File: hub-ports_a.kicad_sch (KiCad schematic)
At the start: 20 parts, among them J3 USB-A, J4 USB-A, U12 TPS2553DBVR, U13 TPS2553DBVR, U16 USBLC6-2SC6, U17 USBLC6-2SC6

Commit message: feat(revc): assign exact BOM and verified local land patterns
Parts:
- C43, C45, C46, C48: footprint (none) -> hub-lib:C_0402_1005Metric; LCSC (none) -> C77020; MPN (none) -> GRM155R71H104KE14D; Manufacturer (none) -> Murata Manufacturing; Ratings (none) -> 50V X7R 10%
- C44, C47: footprint (none) -> hub-lib:CP_Elec_8x6.2; LCSC (none) -> C401648; MPN (none) -> EEEFK1A221P; Manufacturer (none) -> Panasonic Industry; Ratings (none) -> 220uF 10V +/-20%; 8mm diameter, 6.5mm maximum height; polar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
- D8, D9: footprint Diode_SMD:D_SOD-523 -> hub-lib:D_SOD-523; LCSC (none) -> C19950551; Ratings (none) -> See exact manufacturer datasheet
- J3, J4: footprint Connector_USB:USB_A_Wuerth_614004134726_Horizontal -> hub-lib:USB_A_Wuerth_614004134726_Horizontal; Ratings (none) -> See exact manufacturer datasheet
- R101, R102, R47, R48: footprint (none) -> hub-lib:R_0402_1005Metric; LCSC (none) -> C192169; MPN (none) -> ERJ2RKF1003X; Manufacturer (none) -> Panasonic Industry; Ratings (none) -> 1%, 0.1W, 50V
- R38, R39: footprint (none) -> hub-lib:R_0402_1005Metric; LCSC (none) -> C416544; MPN (none) -> ERJ2RKF4642X; Manufacturer (none) -> Panasonic Industry; Ratings (none) -> 1%, 0.1W, 50V
- U12, U13: footprint (none) -> hub-lib:SOT-23-6; LCSC (none) -> C55266; Ratings (none) -> See exact manufacturer datasheet
- U16, U17: footprint Package_TO_SOT_SMD:SOT-23-6 -> hub-lib:SOT-23-6; LCSC (none) -> C7519; Ratings (none) -> See exact manufacturer datasheet

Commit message: feat(revc): place synchronized unrouted board and correct bus startup
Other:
- note added: "Port 1: USB-A, 500 mA with qualified external power"
- note added: "Port 2: USB-A, 500 mA with qualified external power"
- note added: "USB 2.0 / 480 Mbps | Rev C electrical design | Placement and routing review pending"
- note removed: "Rev C | all routing reserved for Alex | electrical draft under review"
- moved on the sheet: C43, C44, C45, C46, C47, C48, D8, D9, J3, J4, R101, R102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

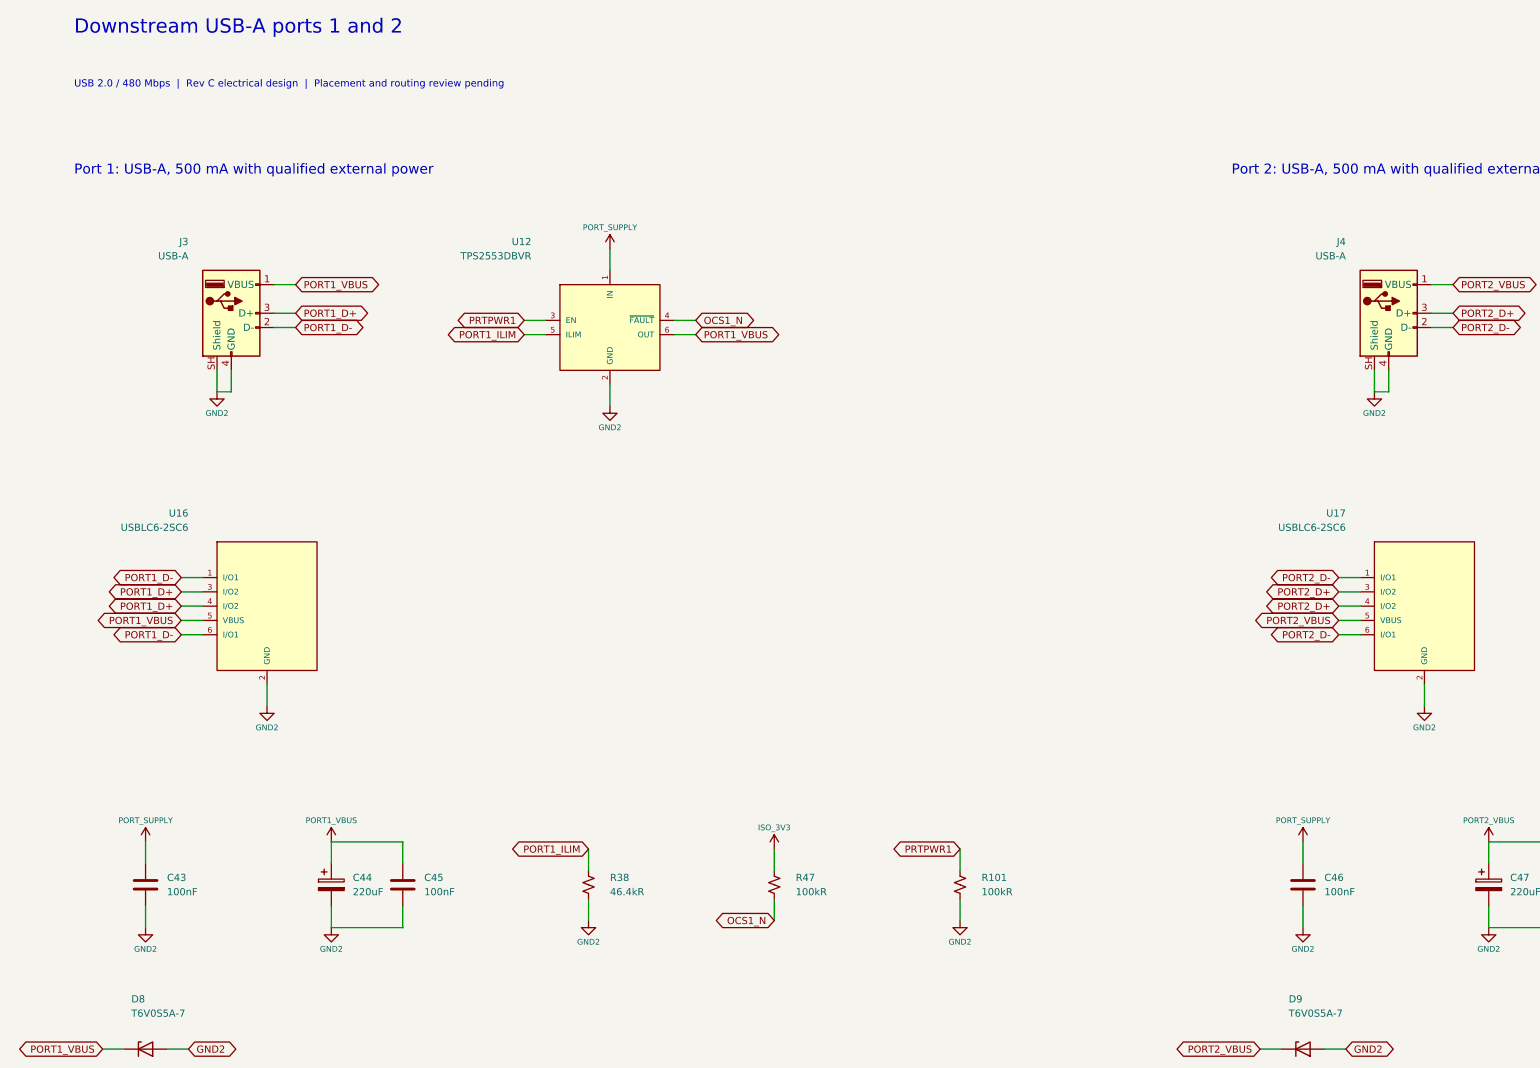
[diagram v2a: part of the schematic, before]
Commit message: feat(revc): finish verified TI hub routing handoff
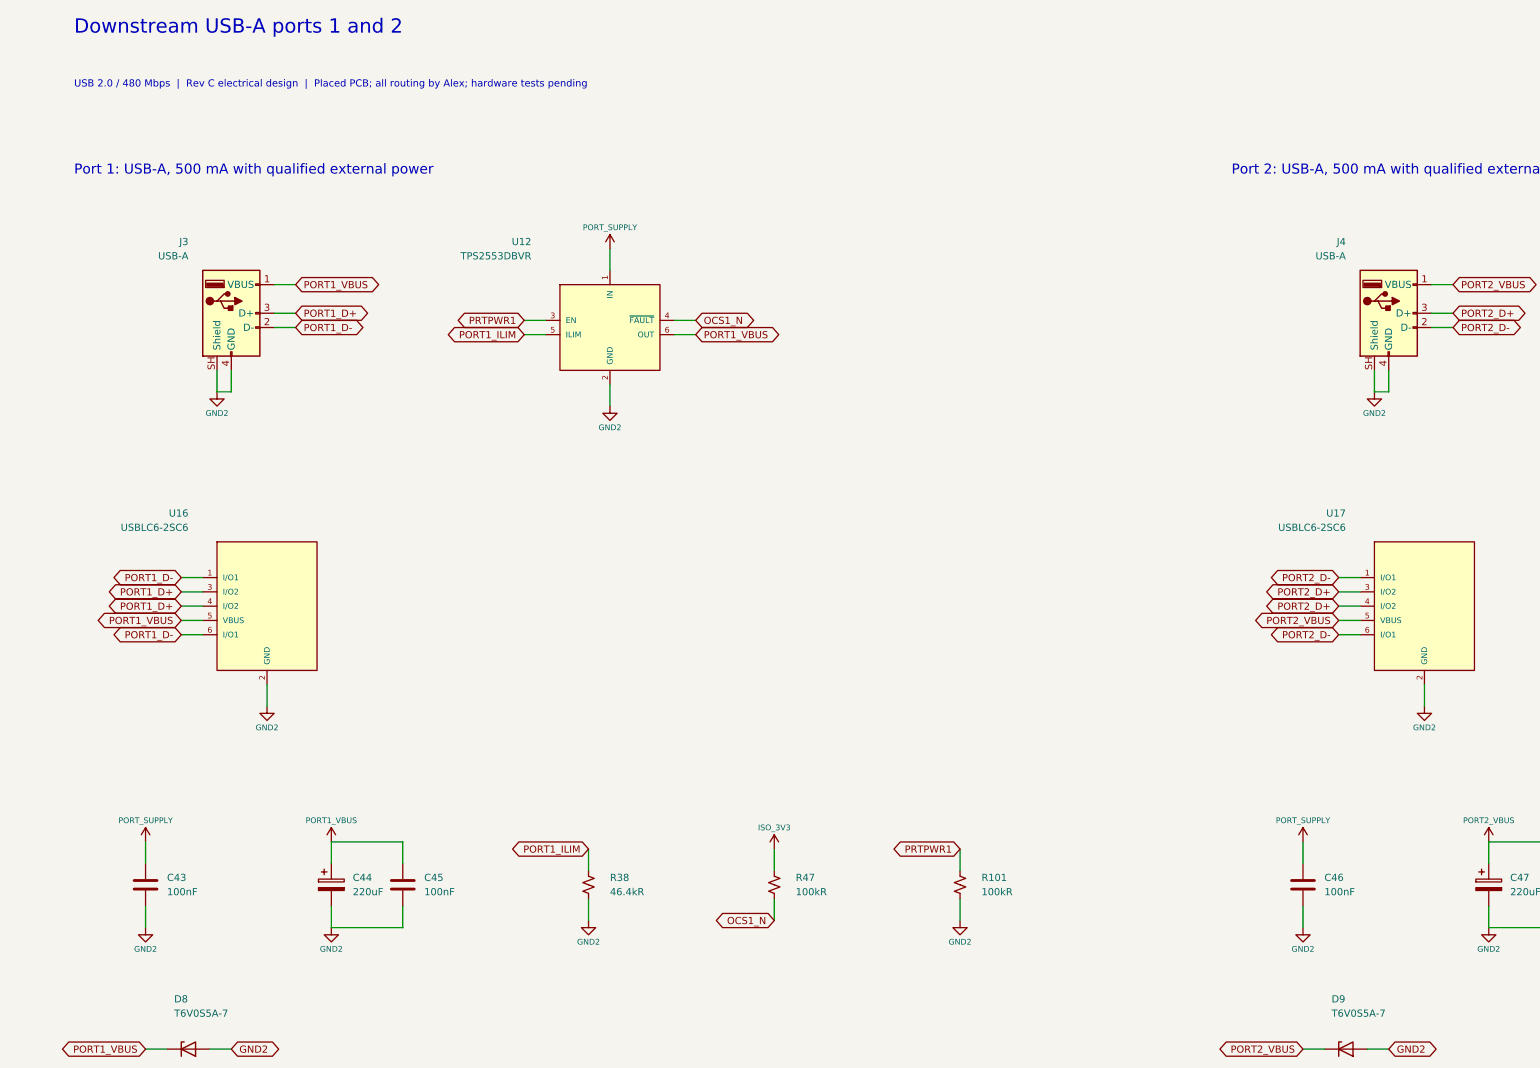
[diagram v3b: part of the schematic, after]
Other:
- note added: "USB 2.0 / 480 Mbps | Rev C electrical design | Placed PCB; all routing by Alex; hardware tests pending"
- note removed: "USB 2.0 / 480 Mbps | Rev C electrical design | Placement and routing review pending"
- moved on the sheet: D8, D9
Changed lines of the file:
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@@
     )
   )
-  (text "USB 2.0 / 480 Mbps  |  Rev C electrical design  |  Placement and routing review pending"
+  (text "USB 2.0 / 480 Mbps  |  Rev C electrical design  |  Placed PCB; all routing by Alex; hardware tests pending"
     (at 20.32 27.94 0)
     (effects
@@
   )
   (symbol
-    (lib_id "hub-lib:power_PORT_SUPPLY")
-    (at 115.57 57.15 0)
+    (lib_id "hub-lib:power_GND2")
+    (at 115.57 85.09 0)
     (unit 1)
     (in_bom no)
@@
     (dnp no)
     (property "Reference" "#PWR9002"
-      (at 115.57 57.15 0)
+      (at 115.57 85.09 0)
       (effects
         (font
@@
       )
     )
-    (property "Value" "PORT_SUPPLY"
-      (at 115.57 53.339999999999996 0)
+    (property "Value" "GND2"
+      (at 115.57 88.9 0)
       (effects
         (font
@@
   )
   (symbol
-    (lib_id "hub-lib:power_GND2")
-    (at 115.57 85.09 0)
+    (lib_id "hub-lib:power_PORT_SUPPLY")
+    (at 115.57 57.15 0)
     (unit 1)
     (in_bom no)
@@
     (dnp no)
     (property "Reference" "#PWR9003"
-      (at 115.57 85.09 0)
+      (at 115.57 57.15 0)
       (effects
         (font
@@
       )
     )
-    (property "Value" "GND2"
-      (at 115.57 88.9 0)
+    (property "Value" "PORT_SUPPLY"
+      (at 115.57 53.339999999999996 0)
       (effects
         (font
@@
   (symbol
     (lib_id "hub-lib:Device_D_Zener")
-    (at 33.02 199.39 0)
+    (at 40.64 199.39 0)
     (unit 1)
     (in_bom yes)
@@
     (dnp no)
     (property "Reference" "D8"
-      (at 30.480000000000004 190.5 0)
+      (at 38.1 190.5 0)
       (effects
         (font
@@
     )
     (property "Value" "T6V0S5A-7"
-      (at 30.480000000000004 193.04 0)
+      (at 38.1 193.04 0)
       (effects
         (font
@@
     )
     (property "Footprint" "hub-lib:D_SOD-523"
-      (at 33.02 199.39 0)
+      (at 40.64 199.39 0)
       (effects
         (font
@@
     )
     (property "Datasheet" "https://www.diodes.com/assets/Datasheets/T6V0S5A.pdf"
-      (at 33.02 199.39 0)
+      (at 40.64 199.39 0)
       (effects
         (font
@@
     )
     (property "Description" "Unidirectional TVS: physical cathode/band pad 1 to VBUS, anode pad 2 to ground"
-      (at 33.02 199.39 0)
+      (at 40.64 199.39 0)
       (effects
         (font
@@
     )
     (property "MPN" "T6V0S5A-7"
-      (at 33.02 199.39 0)
+      (at 40.64 199.39 0)
       (effects
         (font
@@
     )
     (property "Manufacturer" "Diodes Incorporated"
-      (at 33.02 199.39 0)
+      (at 40.64 199.39 0)
       (effects
         (font
@@
     )
     (property "LCSC" "C19950551"
-      (at 33.02 199.39 0)
+      (at 40.64 199.39 0)
       (effects
         (font
@@
     )
     (property "Ratings" "See exact manufacturer datasheet"
-      (at 33.02 199.39 0)
+      (at 40.64 199.39 0)
       (effects
         (font
@@
     )
     (property "CoverMPN" ""
-      (at 33.02 199.39 0)
+      (at 40.64 199.39 0)
       (effects
         (font
@@
     )
     (property "CoverQuantity" ""
-      (at 33.02 199.39 0)
+      (at 40.64 199.39 0)
       (effects
         (font
@@
   (wire
     (pts
-      (xy 29.21 199.39)
-      (xy 25.4 199.39)
+      (xy 36.83 199.39)
+      (xy 33.02 199.39)
     )
     (stroke
@@
   (global_label "PORT1_VBUS"
     (shape bidirectional)
-    (at 25.4 199.39 0)
+    (at 33.02 199.39 0)
     (effects
       (font
@@
     )
     (property "Intersheetrefs" "${INTERSHEET_REFS}"
-      (at 25.4 199.39 0)
+      (at 33.02 199.39 0)
       (effects
         (font
@@
   (wire
     (pts
-      (xy 36.83 199.39)
-      (xy 40.64 199.39)
+      (xy 44.45 199.39)
+      (xy 48.26 199.39)
     )
     (stroke
@@
   (global_label "GND2"
     (shape bidirectional)
-    (at 40.64 199.39 180)
+    (at 48.26 199.39 180)
     (effects
       (font
@@
     )
     (property "Intersheetrefs" "${INTERSHEET_REFS}"
-      (at 40.64 199.39 180)
+      (at 48.26 199.39 180)
       (effects
         (font
@@
   )
   (symbol
-    (lib_id "hub-lib:power_PORT_SUPPLY")
-    (at 321.31 57.15 0)
+    (lib_id "hub-lib:power_GND2")
+    (at 321.31 85.09 0)
     (unit 1)
     (in_bom no)
@@
     (dnp no)
     (property "Reference" "#PWR9013"
-      (at 321.31 57.15 0)
+      (at 321.31 85.09 0)
       (effects
         (font
@@
       )
     )
-    (property "Value" "PORT_SUPPLY"
-      (at 321.31 53.339999999999996 0)
+    (property "Value" "GND2"
+      (at 321.31 88.9 0)
       (effects
         (font
@@
   )
   (symbol
-    (lib_id "hub-lib:power_GND2")
-    (at 321.31 85.09 0)
+    (lib_id "hub-lib:power_PORT_SUPPLY")
+    (at 321.31 57.15 0)
     (unit 1)
     (in_bom no)
@@
     (dnp no)
     (property "Reference" "#PWR9014"
-      (at 321.31 85.09 0)
+      (at 321.31 57.15 0)
       (effects
         (font
@@
       )
     )
-    (property "Value" "GND2"
-      (at 321.31 88.9 0)
+    (property "Value" "PORT_SUPPLY"
+      (at 321.31 53.339999999999996 0)
       (effects
         (font
@@
   (symbol
     (lib_id "hub-lib:Device_D_Zener")
-    (at 238.76 199.39 0)
+    (at 246.38 199.39 0)
     (unit 1)
     (in_bom yes)
@@
     (dnp no)
     (property "Reference" "D9"
-      (at 236.22 190.5 0)
+      (at 243.84 190.5 0)
       (effects
         (font
@@
     )
     (property "Value" "T6V0S5A-7"
-      (at 236.22 193.04 0)
+      (at 243.84 193.04 0)
       (effects
         (font
@@
     )
     (property "Footprint" "hub-lib:D_SOD-523"
-      (at 238.76 199.39 0)
+      (at 246.38 199.39 0)
       (effects
         (font
@@
     )
     (property "Datasheet" "https://www.diodes.com/assets/Datasheets/T6V0S5A.pdf"
-      (at 238.76 199.39 0)
+      (at 246.38 199.39 0)
       (effects
         (font
@@
     )
     (property "Description" "Unidirectional TVS: physical cathode/band pad 1 to VBUS, anode pad 2 to ground"
-      (at 238.76 199.39 0)
+      (at 246.38 199.39 0)
       (effects
         (font
@@
     )
     (property "MPN" "T6V0S5A-7"
-      (at 238.76 199.39 0)
+      (at 246.38 199.39 0)
       (effects
         (font
@@
     )
     (property "Manufacturer" "Diodes Incorporated"
-      (at 238.76 199.39 0)
+      (at 246.38 199.39 0)
       (effects
         (font
@@
     )
     (property "LCSC" "C19950551"
-      (at 238.76 199.39 0)
+      (at 246.38 199.39 0)
       (effects
         (font
@@
     )
     (property "Ratings" "See exact manufacturer datasheet"
-      (at 238.76 199.39 0)
+      (at 246.38 199.39 0)
       (effects
         (font
@@
     )
     (property "CoverMPN" ""
-      (at 238.76 199.39 0)
+      (at 246.38 199.39 0)
       (effects
         (font
@@
     )
     (property "CoverQuantity" ""
-      (at 238.76 199.39 0)
+      (at 246.38 199.39 0)
       (effects
         (font
@@
   (wire
     (pts
-      (xy 234.95 199.39)
-      (xy 231.14 199.39)
+      (xy 242.57 199.39)
+      (xy 238.76 199.39)
     )
     (stroke
@@
   (global_label "PORT2_VBUS"
     (shape bidirectional)
-    (at 231.14 199.39 0)
+    (at 238.76 199.39 0)
     (effects
       (font
@@
     )
     (property "Intersheetrefs" "${INTERSHEET_REFS}"
-      (at 231.14 199.39 0)
+      (at 238.76 199.39 0)
       (effects
         (font
@@
   (wire
     (pts
-      (xy 242.57 199.39)
-      (xy 246.38 199.39)
+      (xy 250.19 199.39)
+      (xy 254.0 199.39)
     )
     (stroke
@@
   (global_label "GND2"
     (shape bidirectional)
-    (at 246.38 199.39 180)
+    (at 254.0 199.39 180)
     (effects
       (font
@@
     )
     (property "Intersheetrefs" "${INTERSHEET_REFS}"
-      (at 246.38 199.39 180)
+      (at 254.0 199.39 180)
       (effects
         (font
